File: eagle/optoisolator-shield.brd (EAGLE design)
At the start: 101.6 x 53.3 mm, 48 parts, among them Q1 NPN, Q2 NPN, Q3 NPN, Q4 NPN, Q5 NPN, Q6 NPN, U1 OPTO, U2 OPTO, U3 OPTO

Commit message: added cam and util directories; routed board, touch-ups still in progress
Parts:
- JP1, JP8: value (none) -> M03_3.5MM
- JP10, JP9: value M023.5MM -> M02_3.5MM
- R1, R10, R11, R12, R13, R14, R15, R16, R17, R18, R2, R3, R4, R5, R6, R7, R8, R9: device SparkFun:C0402 -> SparkFun-Passives:0603-RES
- moved R7 31.5 mm to (12.7, 37.2)
- moved R13 31.5 mm to (54.4, 12.2)
- moved INPUT1 31.0 mm to (80.8, 10.9)
- moved R9 30.8 mm to (12.2, 44.2)
- moved INPUT4 30.5 mm to (80.8, 43.2)
- moved R11 26.3 mm to (29.0, 46.2), turned to 180 degrees
- moved R12 25.1 mm to (29.0, 41.7)
- moved Q1 21.5 mm to (37.6, 22.1), turned to 270 degrees
- moved R8 19.7 mm to (29.7, 38.6)
- moved R3 19.5 mm to (13.6, 25.7)
- moved R10 18.4 mm to (25.4, 36.1)
- moved Q3 17.4 mm to (37.8, 45.2), turned to 270 degrees
- moved Q6 16.9 mm to (17.6, 12.2), turned to 90 degrees
- moved U2 16.6 mm to (20.6, 40.9), turned to 270 degrees
- moved OUTPUT2 15.7 mm to (46.2, 27.4), turned to 90 degrees
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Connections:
- net !ADC_RESET_1 renamed N$601
- removed net AGND: JP4.35, JP4.36, SPI1.6
- removed net IN6: OUTPUT2.10, OUTPUT2.12, OUTPUT2.14, OUTPUT2.16, OUTPUT2.2, OUTPUT2.4, OUTPUT2.6, OUTPUT2.8
- new net GND1: SPI1.6
- new net N$602: JP4.35, JP4.36
- net OPTO_IN6: now also OUTPUT2.10, OUTPUT2.12, OUTPUT2.14, OUTPUT2.16, OUTPUT2.2, OUTPUT2.4, OUTPUT2.6, OUTPUT2.8
- net OUT5: now also JP9.2
- net OUT6: now also JP10.2
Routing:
- net D41: track 0.00 -> 98.2 mm, vias 0 -> 3
- net D38: track 0.00 -> 97.2 mm, vias 0 -> 1
- net D44: track 0.00 -> 94.9 mm, vias 0 -> 1
- net D39: track 0.00 -> 92.6 mm
- net D42: track 0.00 -> 90.5 mm, vias 0 -> 2
- net D40: track 0.00 -> 89.3 mm, vias 0 -> 3
- net D45: track 0.00 -> 88.0 mm, vias 0 -> 2
- net OPTO_OUT3: track 0.00 -> 84.5 mm
- net D43: track 0.00 -> 84.0 mm, vias 0 -> 1
- net OPTO_OUT2: track 0.00 -> 77.1 mm, vias 0 -> 2
- net OPTO_OUT1: track 0.00 -> 76.1 mm, vias 0 -> 1
- net OPTO_OUT4: track 0.00 -> 63.4 mm
- net EXT_VCC: track 0.00 -> 50.0 mm
- net EXT_GND_2: track 0.00 -> 35.5 mm, vias 0 -> 1
- net GND: track 0.00 -> 33.9 mm, vias 0 -> 5
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- added copper zone on layer 1, net D40
- added copper zone on layer 1, net D43
- added copper zone on layer 1, net D44
- added copper zone on layer 1, net EXT_GND_0
- added copper zone on layer 1, net EXT_GND_1
- added copper zone on layer 1, net EXT_GND_2
- added copper zone on layer 1, net EXT_VCC
- added copper zone on layer 16, net GND
- added copper zone on layer 1, net OPTO_OUT3
- added copper zone on layer 1, net OUT1N2
- added copper zone on layer 1, net OUT2N1
- added copper zone on layer 1, net OUT5
- added copper zone on layer 1, net VCC

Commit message: updated board silkscreen to include instructions
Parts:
- added U$1, U$3: (no value), SparkFun-Aesthetics:OSHW-LOGO-L
- added U$4: (no value), creative-commons:CC-BY-SA
- moved R15 1.75 mm to (44.1, 12.7)
- moved R1 1.05 mm to (14.2, 31.5)
- moved R7 0.84 mm to (13.5, 37.1)
- moved R4 0.23 mm to (29.2, 22.4)
- renumbered INPUT1 to INPUT1B, INPUT2 to INPUT2B, INPUT3 to INPUT1C, INPUT4 to INPUT2C, OUTPUT1 to 1A, OUTPUT2 to 2A
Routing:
- net VCC: track 0.00 -> 13.3 mm, vias 0 -> 2
- net OPTO_IN6: track 21.9 -> 23.6 mm
- net EXT_GND_0: track 24.1 -> 25.5 mm
- net N$6: track 5.28 -> 4.21 mm
- net IN1: track 10.7 -> 11.7 mm
- net N$21: track 9.02 -> 8.18 mm
- net IN3: track 7.64 -> 8.45 mm
- net D38: track 97.2 -> 96.7 mm
- net D41: track 98.2 -> 97.7 mm
- added copper zone on layer 16, net D41
- added copper zone on layer 16, net D45
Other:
- board text added: "1A"
- board text added: "1B"
- board text added: "1C"
- board text added: "2A"
- board text added: "2B"
- board text added: "2C"
- board text added: "39"
- board text added: "40"
- board text added: "41"
- board text added: "42"
- board text added: "43"
- board text added: "44"
- board text added: "45"
- board text added: "A"
- board text added: "B"
- board text added: "D38"
- board text added: "GNDA"
- board text added: "GNDB"
- board text added: "GNDC"
- board text added: "INPUT"
- board text added: "OUTPUT"
- board text added: "Place jumper to connect positions A and B. Place at most one jumper per block (D38-D45) to connect the labeled pin to the blocks' input or output."
- board text added: "Released under a Creative Commons Attribution-ShareAlike 4.0 International license (CC-BY-SA 4.0)"
- board text added: "StarCat Optoisolator Shield v1.0"
- board text added: "VCCA"
- board text added: "c 2013 Adam Feuer"

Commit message: updated signal names for optoisolator in/out to match the board silkscreen labels
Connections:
- net OPTO_IN5 renamed OPTO_IN_1A
- net OPTO_IN6 renamed OPTO_IN_2A
- net OPTO_OUT1 renamed OPTO_OUT_1B
- net OPTO_OUT2 renamed OPTO_OUT_2B
- net OPTO_OUT3 renamed OPTO_OUT_1C
- net OPTO_OUT4 renamed OPTO_OUT_2C
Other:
- board text added: "Place jumpers to connect positions A and B. Place at most one jumper per block (D38-D45) to connect the labeled pin to the blocks' input or output."
- board text removed: "Place jumper to connect positions A and B. Place at most one jumper per block (D38-D45) to connect the labeled pin to the blocks' input or output."
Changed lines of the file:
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@@
 <wire x1="8.382" y1="8.382" x2="11.3284" y2="8.382" width="0.254" layer="21"/>
 <wire x1="11.3284" y1="8.382" x2="11.3284" y2="13.0556" width="0.254" layer="21"/>
-<text x="66.3194" y="48.2854" size="0.889" layer="21" rot="R180">Place jumper to connect
+<text x="66.3194" y="48.2854" size="0.889" layer="21" rot="R180">Place jumpers to connect
 positions A and B.
 Place at most one jumper
@@
 </polygon>
 </signal>
-<signal name="OPTO_OUT1">
+<signal name="OPTO_OUT_1B">
 <contactref element="Q2" pad="3"/>
 <contactref element="R6" pad="1"/>
@@
 <via x="40.64" y="17.272" extent="1-16" drill="0.6096"/>
 </signal>
-<signal name="OPTO_OUT2">
+<signal name="OPTO_OUT_2B">
 <contactref element="Q1" pad="3"/>
 <contactref element="R5" pad="1"/>
@@
 <wire x1="73.152" y1="18.288" x2="71.12" y2="15.24" width="0.254" layer="1"/>
 </signal>
-<signal name="OPTO_OUT3">
+<signal name="OPTO_OUT_1C">
 <contactref element="Q4" pad="3"/>
 <contactref element="R12" pad="1"/>
@@
 </polygon>
 </signal>
-<signal name="OPTO_OUT4">
+<signal name="OPTO_OUT_2C">
 <contactref element="Q3" pad="3"/>
 <contactref element="R11" pad="1"/>
@@
 <wire x1="71.5645" y1="45.212" x2="38.946" y2="45.212" width="0.254" layer="1"/>
 </signal>
-<signal name="OPTO_IN5">
+<signal name="OPTO_IN_1A">
 <contactref element="R13" pad="1"/>
 <contactref element="1A" pad="2"/>
@@
 <wire x1="53.594" y1="28.702" x2="53.594" y2="31.242" width="0.254" layer="1"/>
 </signal>
-<signal name="OPTO_IN6">
+<signal name="OPTO_IN_2A">
 <contactref element="R15" pad="2"/>
 <contactref element="2A" pad="2"/>

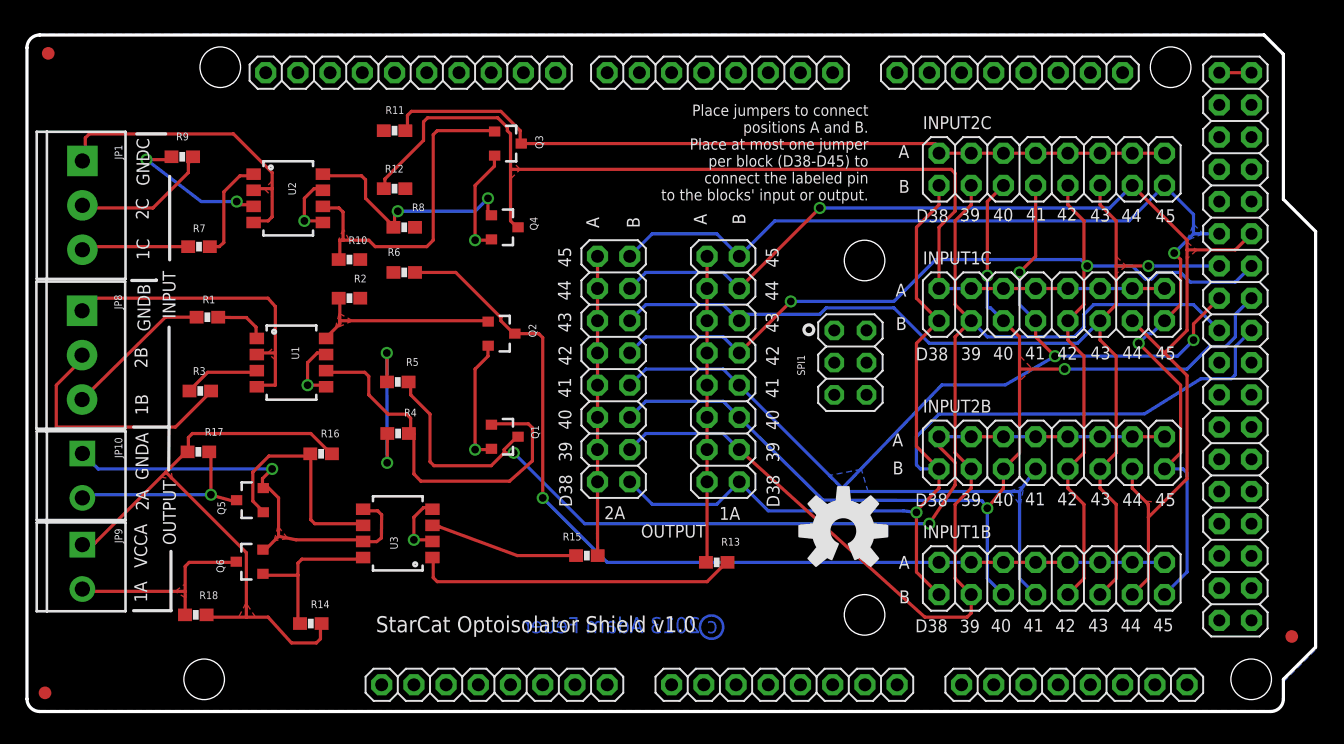
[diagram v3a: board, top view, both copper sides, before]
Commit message: corrected board outline positioning to make origin at 0,0; added creative-commons logo library
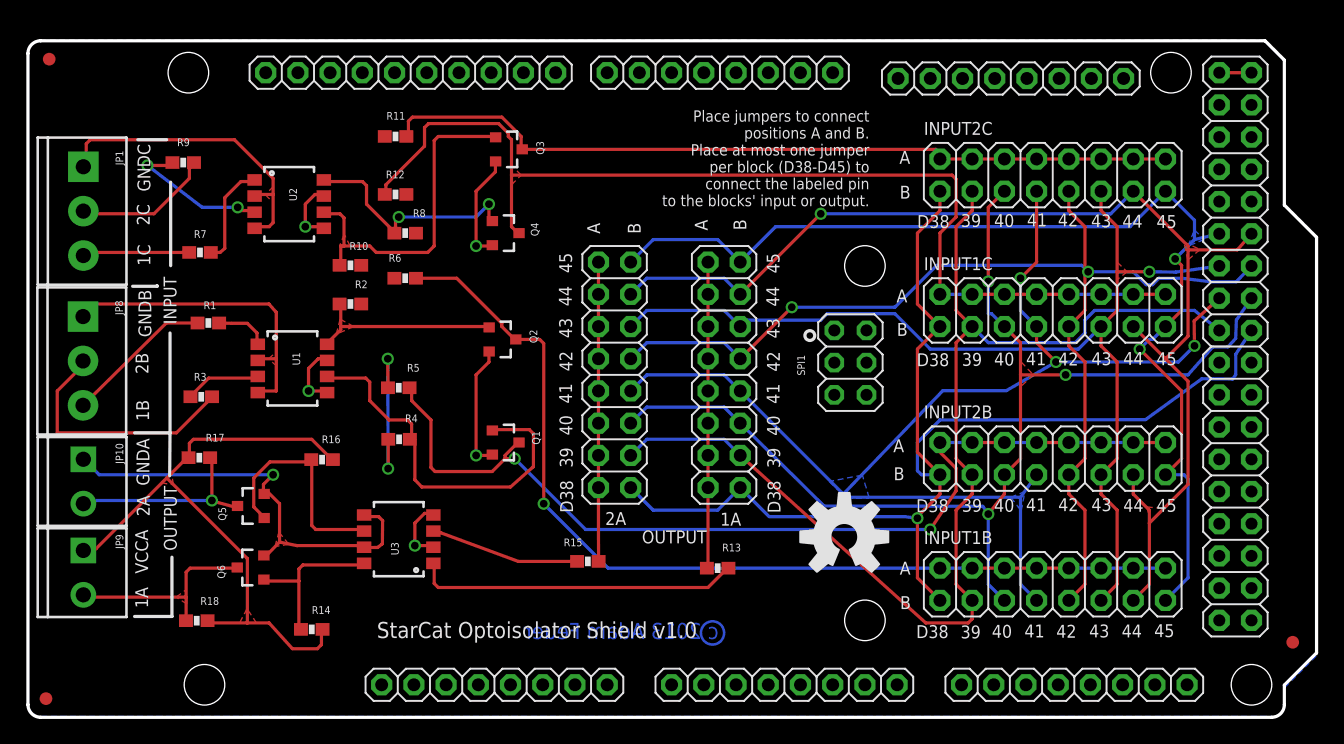
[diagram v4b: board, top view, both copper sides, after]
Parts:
- moved JP8 0.46 mm to (4.39, 31.6)
- moved 1A 0.46 mm to (54.9, 27.0)
- moved 2A 0.46 mm to (46.3, 27.0)
- moved INPUT1B 0.46 mm to (80.8, 10.5)
- moved INPUT1C 0.46 mm to (80.8, 32.1)
- moved INPUT2B 0.46 mm to (80.8, 20.4)
- moved INPUT2C 0.46 mm to (80.8, 42.7)
- moved JP1 0.46 mm to (4.42, 43.4)
- moved JP10 0.46 mm to (4.42, 20.3)
- moved JP3 0.46 mm to (77.5, 50.3)
- moved JP9 0.46 mm to (4.42, 13.1)
- moved Q1 0.46 mm to (37.7, 21.6)
- moved Q2 0.46 mm to (37.4, 29.8)
- moved Q3 0.46 mm to (37.9, 44.8)
- moved Q4 0.46 mm to (37.7, 38.2)
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
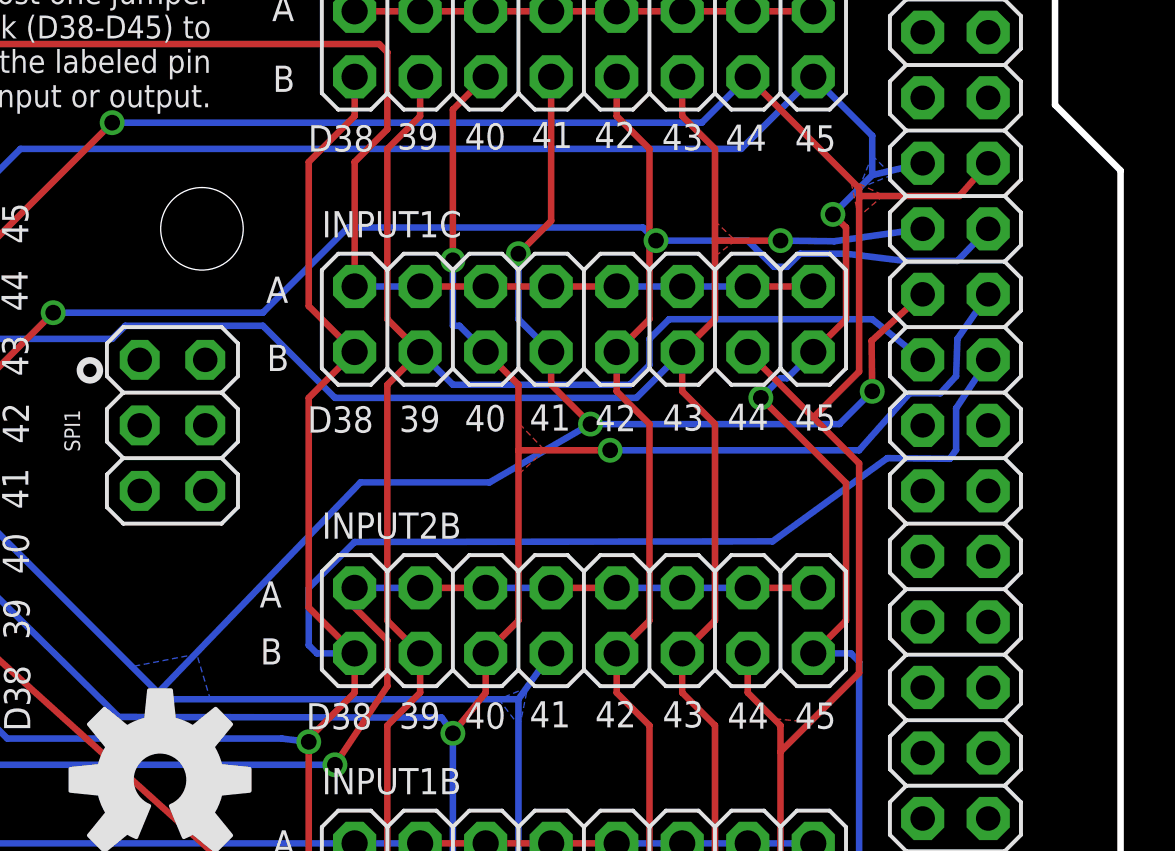
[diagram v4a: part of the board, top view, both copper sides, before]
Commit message: improved some trace clearances by rerouting them
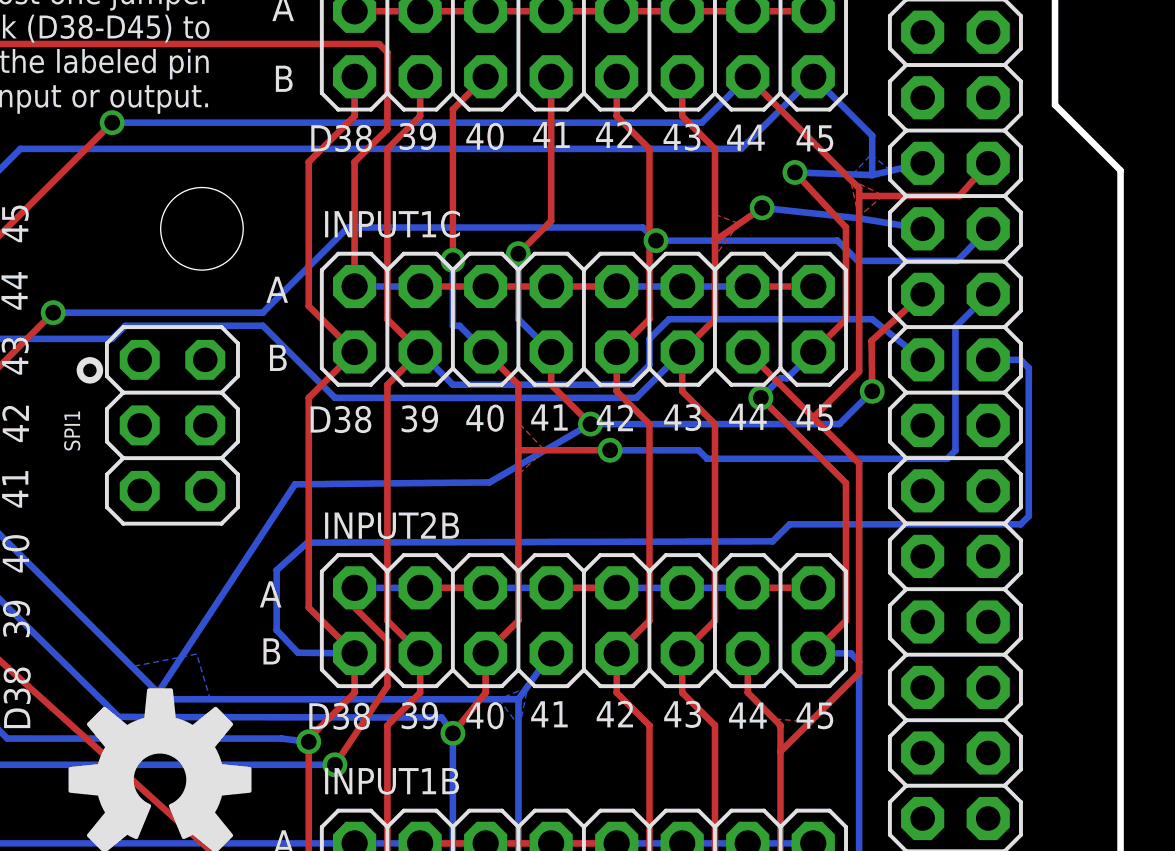
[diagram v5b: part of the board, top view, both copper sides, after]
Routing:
- net D38: track 96.8 -> 104.9 mm
- net D45: track 87.7 -> 90.8 mm
- net D40: track 89.5 -> 91.5 mm
- net D41: track 98.2 -> 99.1 mm
